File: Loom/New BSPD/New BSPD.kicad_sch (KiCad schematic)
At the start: 17 parts, among them J1 Conn_01x03, J2 Conn_01x03, J3 Conn_01x03, K1 MCCMA51-S-DC12V-C, Q1 IRLZ44Z, U1 4011, U2 4011, X1 ASZKDV-32.768KHz

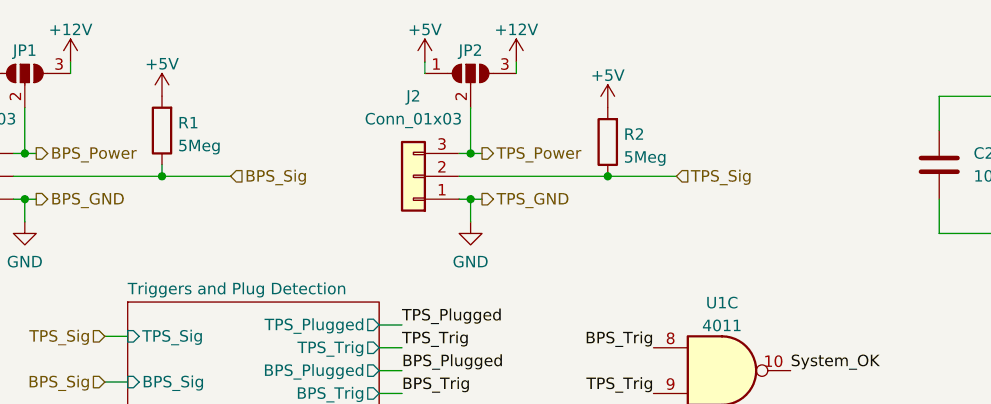
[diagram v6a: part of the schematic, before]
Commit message: Add test points
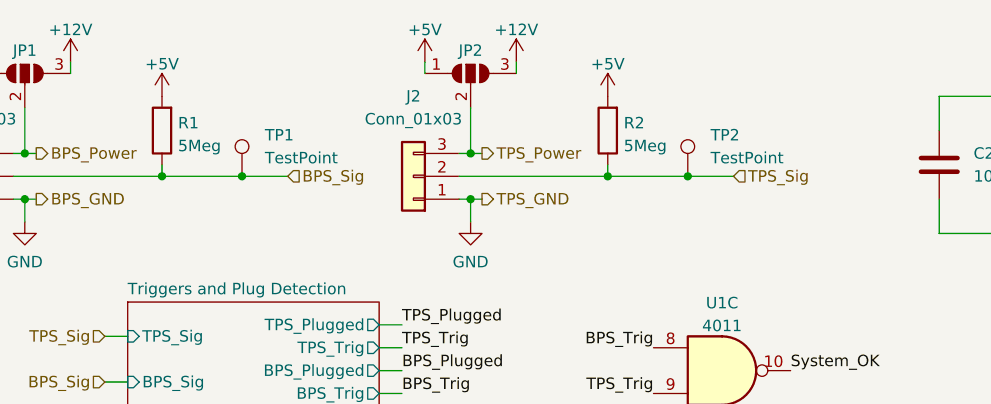
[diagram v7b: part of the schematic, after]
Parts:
- added TP1, TP2: TestPoint, TestPoint:TestPoint_THTPad_D3.0mm_Drill1.5mm, symbol Connector:TestPoint
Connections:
- net BPS_Sig: now also TP1.1
- net TPS_Sig: now also TP2.1
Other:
- moved on the sheet: R2
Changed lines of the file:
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@@
 (kicad_sch (version 20230121) (generator eeschema)
   (paper "A4")
+  (junction (at 62.23 38.1) (diameter 0) (color 0 0 0 0)
+  )
   (junction (at 227.33 79.375) (diameter 0) (color 0 0 0 0)
   )
   (junction (at 38.1 40.64) (diameter 0) (color 0 0 0 0)
   )
+  (junction (at 111.76 38.1) (diameter 0) (color 0 0 0 0)
+  )
   (junction (at 53.34 38.1) (diameter 0) (color 0 0 0 0)
   )
@@
     (stroke (width 0) (type default))
   )
+  (wire (pts (xy 111.76 38.1) (xy 116.84 38.1))
+    (stroke (width 0) (type default))
+  )
   (wire (pts (xy 36.83 38.1) (xy 53.34 38.1))
     (stroke (width 0) (type default))
@@
     (stroke (width 0) (type default))
   )
+  (wire (pts (xy 62.23 38.1) (xy 67.31 38.1))
+    (stroke (width 0) (type default))
+  )
   (wire (pts (xy 222.885 78.105) (xy 222.885 79.375))
     (stroke (width 0) (type default))
@@
     (stroke (width 0) (type default))
   )
-  (wire (pts (xy 102.87 38.1) (xy 110.49 38.1))
+  (wire (pts (xy 102.87 38.1) (xy 111.76 38.1))
+    (stroke (width 0) (type default))
+  )
+  (wire (pts (xy 102.87 36.83) (xy 102.87 38.1))
     (stroke (width 0) (type default))
   )
@@
     (stroke (width 0) (type default))
   )
-  (wire (pts (xy 53.34 38.1) (xy 60.96 38.1))
+  (wire (pts (xy 53.34 38.1) (xy 62.23 38.1))
     (stroke (width 0) (type default))
   )
@@
     (effects (font (size 1.27 1.27)) (justify left))
   )
-  (hierarchical_label "BPS_Sig" (shape input) (at 60.96 38.1 0) (fields_autoplaced)
+  (hierarchical_label "BPS_Sig" (shape input) (at 67.31 38.1 0) (fields_autoplaced)
     (effects (font (size 1.27 1.27)) (justify left))
   )
@@
     (effects (font (size 1.27 1.27)) (justify right))
   )
-  (hierarchical_label "TPS_Sig" (shape input) (at 110.49 38.1 0) (fields_autoplaced)
+  (hierarchical_label "TPS_Sig" (shape input) (at 116.84 38.1 0) (fields_autoplaced)
     (effects (font (size 1.27 1.27)) (justify left))
   )
@@
     )
   )
+  (symbol (lib_id "Connector:TestPoint") (at 62.23 38.1 0) (unit 1)
+    (in_bom yes) (on_board yes) (dnp no) (fields_autoplaced)
+    (property "Reference" "TP1" (at 64.77 33.528 0)
+      (effects (font (size 1.27 1.27)) (justify left))
+    )
+    (property "Value" "TestPoint" (at 64.77 36.068 0)
+      (effects (font (size 1.27 1.27)) (justify left))
+    )
+    (property "Footprint" "TestPoint:TestPoint_THTPad_D3.0mm_Drill1.5mm" (at 67.31 38.1 0)
+      (effects (font (size 1.27 1.27)) hide)
+    )
+    (property "Datasheet" "~" (at 67.31 38.1 0)
+      (effects (font (size 1.27 1.27)) hide)
+    )
+    (pin "1")
+    (instances
+      (project "New BSPD"
+        (path "/1f7c501a-057f-4634-92ce-528b01503799"
+          (reference "TP1") (unit 1)
+        )
+      )
+    )
+  )
   (symbol (lib_id "power:GND") (at 87.63 43.18 0) (unit 1)
     (in_bom yes) (on_board yes) (dnp no) (fields_autoplaced)
@@
     )
   )
-  (symbol (lib_id "power:+5V") (at 102.87 30.48 0) (unit 1)
-    (in_bom yes) (on_board yes) (dnp no) (fields_autoplaced)
-    (property "Reference" "#PWR06" (at 102.87 34.29 0)
-      (effects (font (size 1.27 1.27)) hide)
-    )
-    (property "Value" "+5V" (at 102.87 26.9042 0)
-      (effects (font (size 1.27 1.27)))
-    )
-    (property "Footprint" "" (at 102.87 30.48 0)
-      (effects (font (size 1.27 1.27)) hide)
-    )
-    (property "Datasheet" "" (at 102.87 30.48 0)
+  (symbol (lib_id "power:+5V") (at 102.87 29.21 0) (unit 1)
+    (in_bom yes) (on_board yes) (dnp no) (fields_autoplaced)
+    (property "Reference" "#PWR06" (at 102.87 33.02 0)
+      (effects (font (size 1.27 1.27)) hide)
+    )
+    (property "Value" "+5V" (at 102.87 25.6342 0)
+      (effects (font (size 1.27 1.27)))
+    )
+    (property "Footprint" "" (at 102.87 29.21 0)
+      (effects (font (size 1.27 1.27)) hide)
+    )
+    (property "Datasheet" "" (at 102.87 29.21 0)
       (effects (font (size 1.27 1.27)) hide)
     )
@@
     )
   )
-  (symbol (lib_id "Device:R") (at 102.87 34.29 180) (unit 1)
-    (in_bom yes) (on_board yes) (dnp no) (fields_autoplaced)
-    (property "Reference" "R2" (at 104.648 33.4553 0)
+  (symbol (lib_id "Device:R") (at 102.87 33.02 180) (unit 1)
+    (in_bom yes) (on_board yes) (dnp no) (fields_autoplaced)
+    (property "Reference" "R2" (at 104.648 32.1853 0)
       (effects (font (size 1.27 1.27)) (justify right))
     )
-    (property "Value" "5Meg" (at 104.648 35.9922 0)
+    (property "Value" "5Meg" (at 104.648 34.7222 0)
       (effects (font (size 1.27 1.27)) (justify right))
     )
-    (property "Footprint" "Resistor_THT:R_Axial_DIN0207_L6.3mm_D2.5mm_P7.62mm_Horizontal" (at 104.648 34.29 90)
-      (effects (font (size 1.27 1.27)) hide)
-    )
-    (property "Datasheet" "~" (at 102.87 34.29 0)
+    (property "Footprint" "Resistor_THT:R_Axial_DIN0207_L6.3mm_D2.5mm_P7.62mm_Horizontal" (at 104.648 33.02 90)
+      (effects (font (size 1.27 1.27)) hide)
+    )
+    (property "Datasheet" "~" (at 102.87 33.02 0)
       (effects (font (size 1.27 1.27)) hide)
     )
@@
         )
       )
+    )
+  )
+  (symbol (lib_id "Connector:TestPoint") (at 111.76 38.1 0) (unit 1)
+    (in_bom yes) (on_board yes) (dnp no) (fields_autoplaced)
+    (property "Reference" "TP2" (at 114.3 33.528 0)
+      (effects (font (size 1.27 1.27)) (justify left))
+    )
+    (property "Value" "TestPoint" (at 114.3 36.068 0)
+      (effects (font (size 1.27 1.27)) (justify left))
+    )
+    (property "Footprint" "TestPoint:TestPoint_THTPad_D3.0mm_Drill1.5mm" (at 116.84 38.1 0)
+      (effects (font (size 1.27 1.27)) hide)
+    )
+    (property "Datasheet" "~" (at 116.84 38.1 0)
+      (effects (font (size 1.27 1.27)) hide)
+    )
+    (pin "1")
+    (instances
+      (project "New BSPD"
+        (path "/1f7c501a-057f-4634-92ce-528b01503799"
+          (reference "TP2") (unit 1)
+        )
+      )

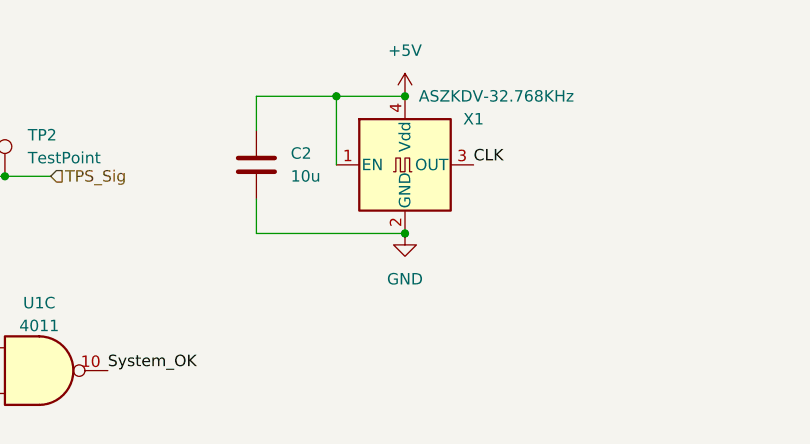
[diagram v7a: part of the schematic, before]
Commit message: Fix BSPD Crystal Footprint
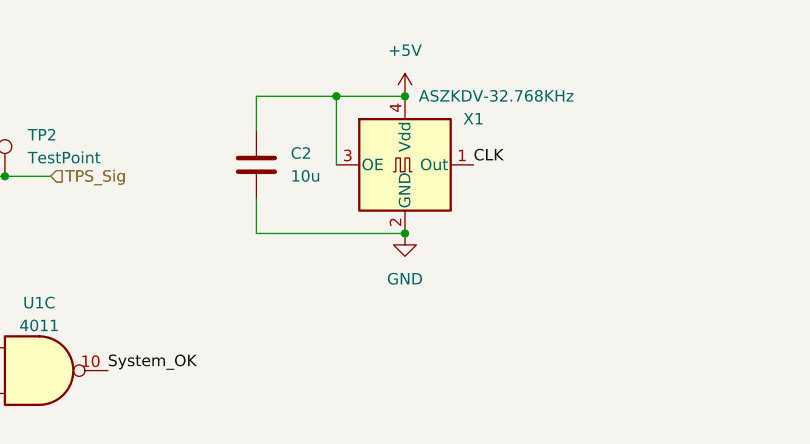
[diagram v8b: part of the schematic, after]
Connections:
- net +5V: now also X1.3 (OE); no longer X1.1 (EN)
- net CLK: now also X1.1 (Out); no longer X1.3 (OUT)
